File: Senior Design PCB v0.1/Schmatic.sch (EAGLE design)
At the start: 231 parts, among them IC1 TMC2208, IC2 TMC2208, IC3 TMC2208, IC4 TMC2208, IC5 TMC2208, IC6 CP2104, Q1 mmbt2222, Q2 mmbt2222, Q3 MMBT4403, Q4 AOD417, Q5 MMBT4403, Q6 MMBT4403, Q7 DMG3415U, U1 PCA9685, U2 AP2112-3.3, U3 HTU21DF, U4 HX711, U5 HX711, U6 HX711, U7 SX1509, X2 ESP32_WROOM32_SKINNY

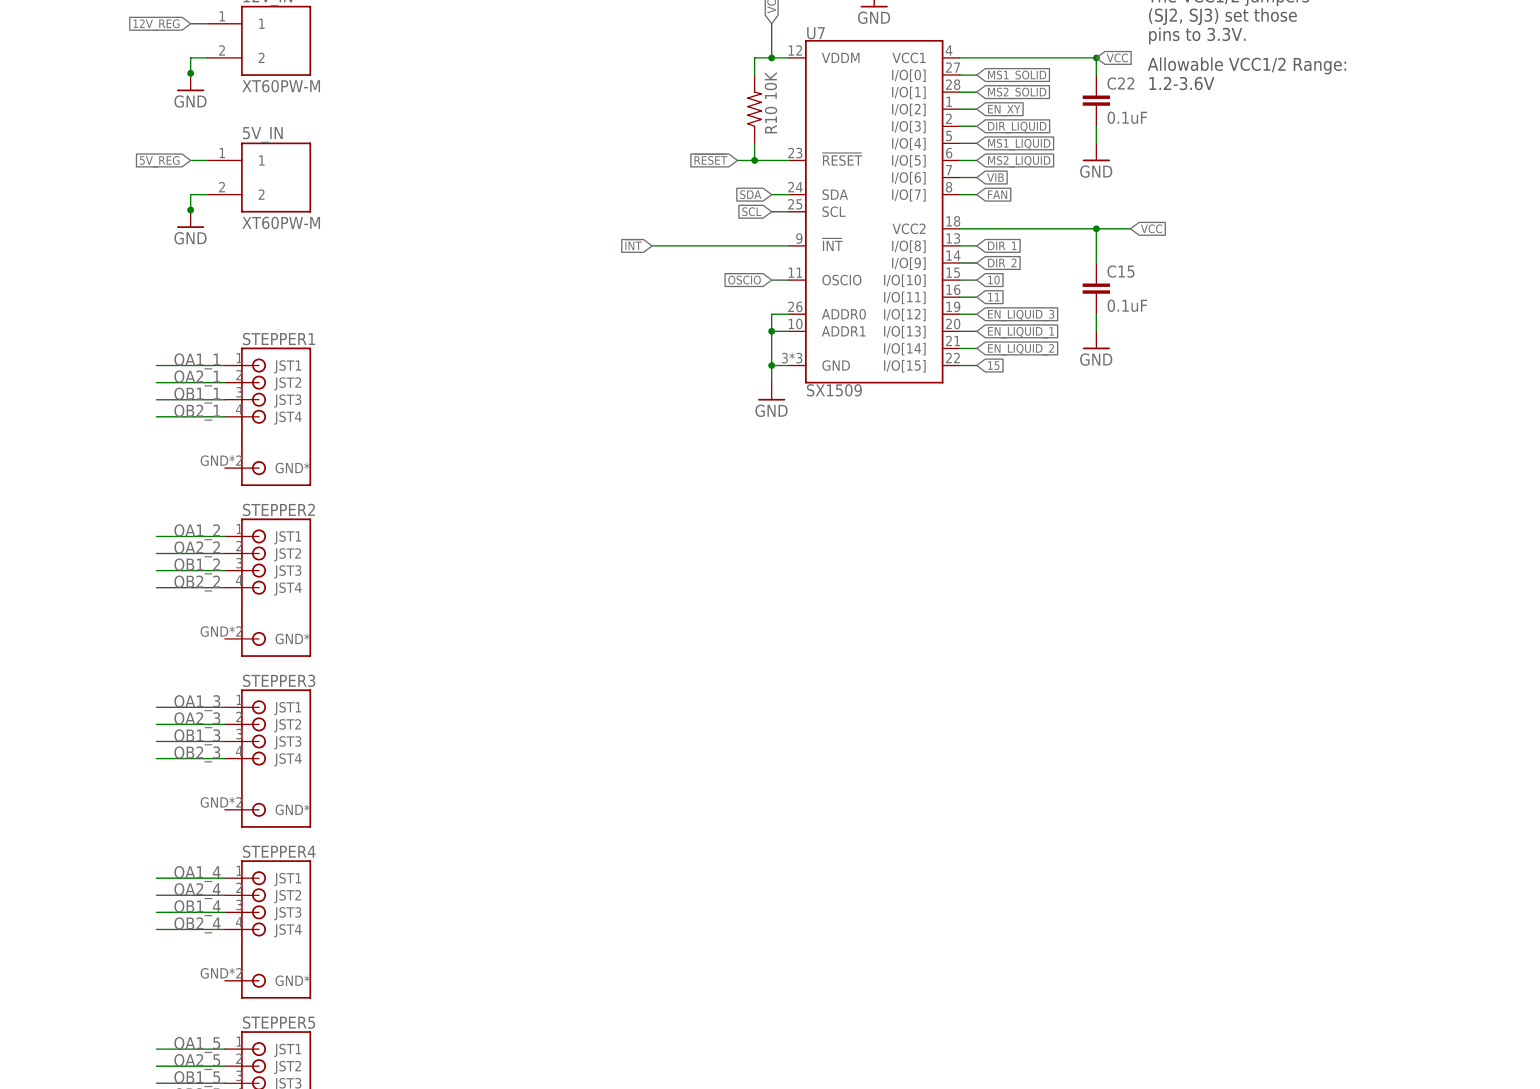
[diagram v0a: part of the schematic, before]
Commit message: added buck 12to5 3A
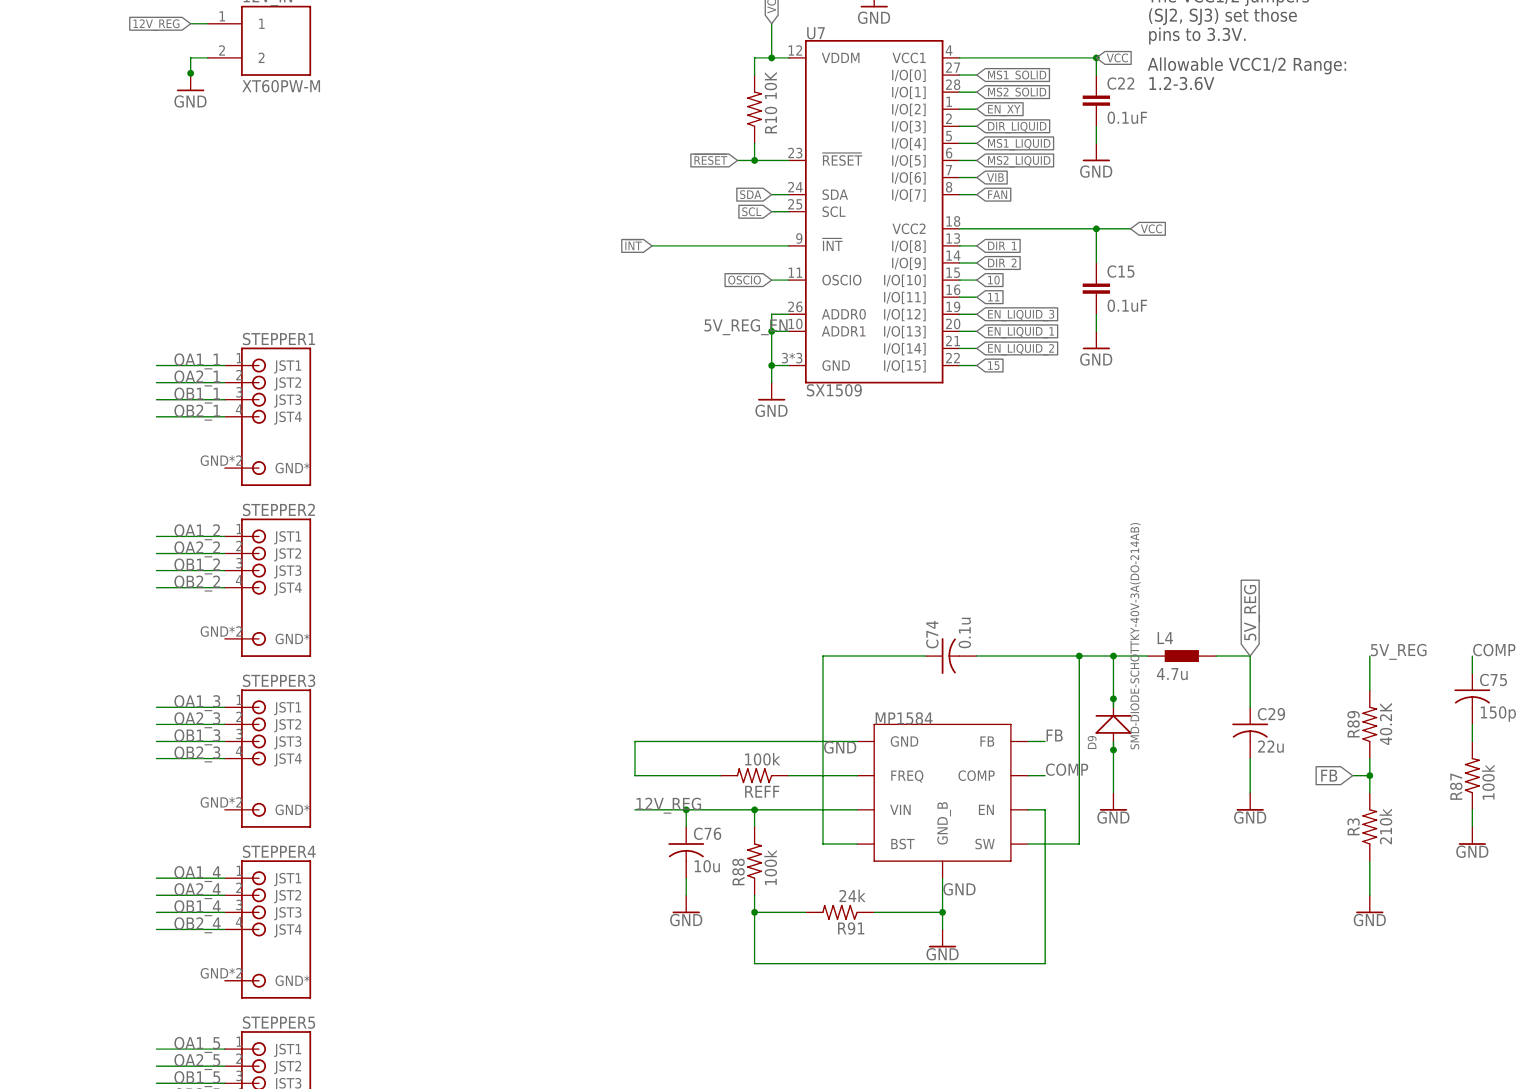
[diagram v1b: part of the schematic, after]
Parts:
- removed 5V_IN: XT60PW-M, XT60PW-M:XT60PW-M
- added C29: 22u, adafruit:C-USC1206
- added C74: 0.1u, adafruit:C-USC0603
- added C75: 150p, adafruit:C-USC0603
- added C76: 10u, adafruit:C-USC1206
- added D9: SMD-DIODE-SCHOTTKY-40V-3A(DO-214AB), SMD-DIODE-SCHOTTKY-40V-3A_DO-214AB_:SMD-DIODE-SCHOTTKY-40V-3A(DO-214AB)
- added L4: 4.7u, NewKevinMade:MHCI0603-4R7M-R8
- added R3: 210k, SparkFun-Resistors:220KOHM-0603-1/10W-1%
- added R87, R88, REFF: 100k, adafruit:R-US_R0603
- added R89: 40.2K, SparkFun-Resistors:RESISTOR0603
- added R91: 24k, adafruit:R-US_R0603
- added U$2: MP1584_V2, mp1584S:MP1584_V2
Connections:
- new net 5V_REG_EN: R88.1, R91.2, U$2.EN
- new net BST: C74.1, U$2.BST
- new net COMP: C75.1, U$2.COMP
- new net FB: R3.2, R89.1, U$2.FB
- new net FREQ: REFF.1, U$2.FREQ
- new net N$10: C75.2, R87.2
- new net SW: C74.2, D9.-, L4.1, U$2.SW
- net 12V_REG: now also C76.1, R88.2, U$2.VIN
- net 5V_REG: now also C29.1, L4.2, R89.2; no longer 5V_IN.1
- net GND: now also C29.2, C76.2, D9.+, R3.1, R87.1, R91.1, REFF.2, U$2.GND, U$2.GND_B; no longer 5V_IN.2

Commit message: added another buck converter for 5v to 3v3
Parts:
- removed C1: 10uF, microbuilder:CAP_CERAMIC0805-NOOUTLINE
- removed C6, C8: 10µF, microbuilder:CAP_CERAMIC0805-NOOUTLINE
- removed C7: 1uF, microbuilder:CAP_CERAMIC0603_NO
- removed R7: 100K, microbuilder:RESISTOR_0603_NOOUT
- removed U2: AP2112-3.3, microbuilder:VREG_SOT23-5
- added C77, C78, C80: 0.1uF, SparkFun-Capacitors:0.1UF-0603-25V-(+80/-20%)
- added C79: 4.7uF, SparkFun-Capacitors:4.7UF-1206-16V-(+80/-20%)
- added D10: 3A/40V/500mV, SparkFun-DiscreteSemi:DIODE-SCHOTTKY-B340A
- added L5: SWPA3012S4R7MT, rcl:L-USL3230M
- added MP2451: MP2451, NewKevinMade:MP2451
- added R92: 100K, SparkFun-Resistors:RESISTOR0603
- added R93: 124K, SparkFun-Resistors:RESISTOR0603
- added R94: 40.2k, SparkFun-Resistors:RESISTOR0603
- R3: value 210k -> 40.2K
- R89: value 40.2K -> 210K
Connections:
- removed net EN: R7.1, U2.EN
- removed net N$26: IC6G$1.VBUS, J2.VBUS
- removed net N$7: C6.1, D4.C, Q7.S, R7.2, U2.IN
- new net 3V3_FB: MP2451.FB, R93.1, R94.2
- new net N$25: MP2451.EN, R92.1
- new net N$29: C77.1, MP2451.BST
- new net N$31: C77.2, D10.C, L5.1, MP2451.SW
- new net VIN: C78.2, D4.C, MP2451.VIN, Q7.S, R92.2
- net GND: now also C78.1, C79.2, C80.1, D10.A, MP2451.GND, R94.1; no longer C1.2, C6.2, C7.2, C8.2, U2.GND
- net VBUS: now also IC6G$1.VBUS, J2.VBUS
- net VCC: now also C79.1, C80.2, L5.2, R93.2; no longer C1.1, C7.1, C8.1, U2.OUT
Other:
- moved on the sheet: D4, Q7
